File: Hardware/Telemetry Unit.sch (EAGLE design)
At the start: 51 parts, among them IC1 MEGA128-A, IC2 FT232RL, J2 503182-1852, J3 10118193-0001LF, Q1 10MHz, U1 MPL3115A2, U2 AP65111A, U3 LSM6DS3

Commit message: Added fuse to usb
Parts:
- added F1: MF-MSMF050-2, MF-MSMF050-2:MF-MSMF050-2
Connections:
- new net N$22: F1.1, J3.VUSB
- net V_USB: now also F1.2; no longer J3.VUSB
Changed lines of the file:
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@@
 <?xml version="1.0" encoding="utf-8"?>
 <!DOCTYPE eagle SYSTEM "eagle.dtd">
-<eagle version="9.2.2">
+<eagle version="9.3.0">
 <drawing>
 <settings>
@@
 <part name="R15" library="resistor" library_urn="urn:adsk.eagle:library:348" deviceset="R-US_" device="R0603" package3d_urn="urn:adsk.eagle:package:23555/3" value="10k"/>
 <part name="R16" library="resistor" library_urn="urn:adsk.eagle:library:348" deviceset="R-US_" device="R0603" package3d_urn="urn:adsk.eagle:package:23555/3" value="10k"/>
+<part name="F1" library="MF-MSMF050-2" deviceset="MF-MSMF050-2" device=""/>
 </parts>
 <sheets>
@@
 <attribute name="VALUE" x="21.59" y="70.358" size="1.778" layer="96"/>
 </instance>
+<instance part="F1" gate="G$1" x="-55.88" y="50.8" smashed="yes">
+<attribute name="NAME" x="-59.69661875" y="52.19943125" size="1.781090625" layer="95"/>
+<attribute name="VALUE" x="-59.696859375" y="47.873740625" size="1.7812" layer="96"/>
+</instance>
 </instances>
 <busses>
@@
 </segment>
 </net>
-<net name="V_USB" class="0">
-<segment>
-<pinref part="J3" gate="G$1" pin="VUSB"/>
-<wire x1="-63.5" y1="50.8" x2="-50.8" y2="50.8" width="0.1524" layer="91"/>
-<label x="-53.34" y="50.8" size="1.778" layer="95" align="bottom-right"/>
-</segment>
-</net>
 <net name="N$11" class="0">
 <segment>
@@
 </segment>
 </net>
+<net name="N$22" class="0">
+<segment>
+<pinref part="J3" gate="G$1" pin="VUSB"/>
+<pinref part="F1" gate="G$1" pin="1"/>
+<wire x1="-63.5" y1="50.8" x2="-60.96" y2="50.8" width="0.1524" layer="91"/>
+</segment>
+</net>
+<net name="V_USB" class="0">
+<segment>
+<pinref part="F1" gate="G$1" pin="2"/>
+<wire x1="-50.8" y1="50.8" x2="-45.72" y2="50.8" width="0.1524" layer="91"/>
+<label x="-48.26" y="50.8" size="1.778" layer="95"/>
+</segment>
+</net>

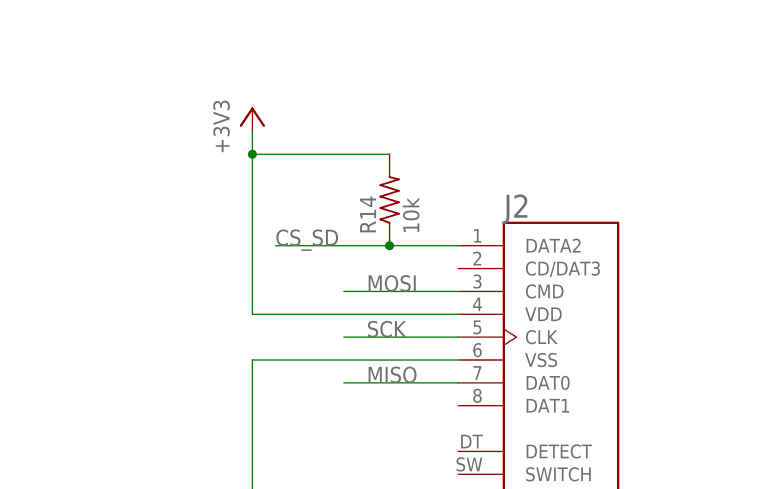
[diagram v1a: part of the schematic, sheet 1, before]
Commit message: Consolidated resistors and capacitors
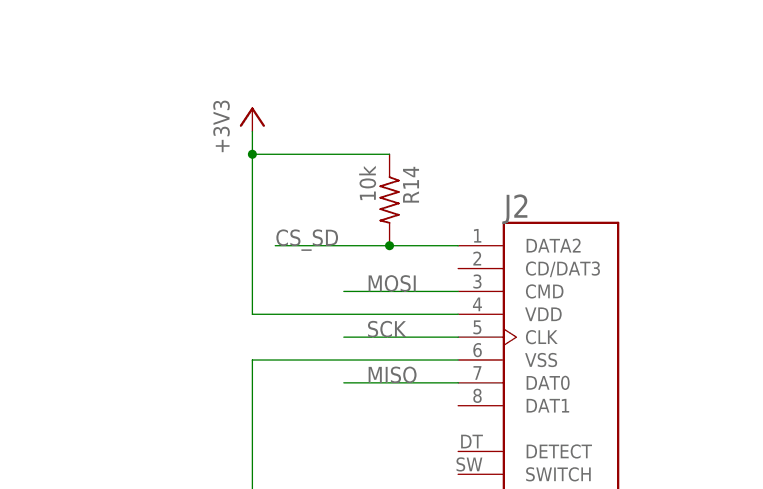
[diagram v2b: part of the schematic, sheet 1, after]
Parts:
- C14: value 100nF -> 100n; device rcl:C-EUC0603 -> resistor:C-USC0603
- R14: device rcl:R-US_R0603 -> resistor:R-US_R0603
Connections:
- net +3V3: now also R14.1; no longer R14.2
- net CS_SD: now also R14.2; no longer R14.1
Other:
- moved on the sheet: R14
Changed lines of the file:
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@@
 <part name="P+2" library="supply1" library_urn="urn:adsk.eagle:library:371" deviceset="+3V3" device=""/>
 <part name="GND17" library="supply1" library_urn="urn:adsk.eagle:library:371" deviceset="GND" device=""/>
-<part name="C14" library="rcl" library_urn="urn:adsk.eagle:library:334" deviceset="C-EU" device="C0603" package3d_urn="urn:adsk.eagle:package:23616/2" value="100nF"/>
 <part name="R12" library="rcl" library_urn="urn:adsk.eagle:library:334" deviceset="R-US_" device="R0603" package3d_urn="urn:adsk.eagle:package:23555/2" value="1k"/>
 <part name="R13" library="rcl" library_urn="urn:adsk.eagle:library:334" deviceset="R-US_" device="R0603" package3d_urn="urn:adsk.eagle:package:23555/2" value="1k"/>
@@
 <part name="P+3" library="supply1" library_urn="urn:adsk.eagle:library:371" deviceset="+3V3" device=""/>
 <part name="P+4" library="supply1" library_urn="urn:adsk.eagle:library:371" deviceset="+3V3" device=""/>
-<part name="R14" library="rcl" library_urn="urn:adsk.eagle:library:334" deviceset="R-US_" device="R0603" package3d_urn="urn:adsk.eagle:package:23555/2" value="10k"/>
 <part name="GND18" library="supply1" library_urn="urn:adsk.eagle:library:371" deviceset="GND" device=""/>
 <part name="JP1" library="pinhead" library_urn="urn:adsk.eagle:library:325" deviceset="PINHD-2X3" device="" package3d_urn="urn:adsk.eagle:package:22462/2"/>
@@
 <part name="R16" library="resistor" library_urn="urn:adsk.eagle:library:348" deviceset="R-US_" device="R0603" package3d_urn="urn:adsk.eagle:package:23555/3" value="10k"/>
 <part name="F1" library="MF-MSMF050-2" deviceset="MF-MSMF050-2" device=""/>
+<part name="R14" library="resistor" library_urn="urn:adsk.eagle:library:348" deviceset="R-US_" device="R0603" package3d_urn="urn:adsk.eagle:package:23555/3" value="10k"/>
+<part name="C14" library="resistor" library_urn="urn:adsk.eagle:library:348" deviceset="C-US" device="C0603" package3d_urn="urn:adsk.eagle:package:23616/2" value="100n"/>
 </parts>
 <sheets>
@@
 <attribute name="VALUE" x="127" y="68.58" size="1.778" layer="96"/>
 </instance>
-<instance part="R14" gate="G$1" x="144.78" y="116.84" smashed="yes" rot="R90">
-<attribute name="NAME" x="143.2814" y="113.03" size="1.778" layer="95" rot="R90"/>
-<attribute name="VALUE" x="148.082" y="113.03" size="1.778" layer="96" rot="R90"/>
+<instance part="R14" gate="G$1" x="144.78" y="116.84" smashed="yes" rot="R270">
+<attribute name="NAME" x="146.2786" y="120.65" size="1.778" layer="95" rot="R270"/>
+<attribute name="VALUE" x="141.478" y="120.65" size="1.778" layer="96" rot="R270"/>
 </instance>
 </instances>
@@
 <pinref part="+3V9" gate="G$1" pin="+3V3"/>
 <wire x1="129.54" y1="104.14" x2="129.54" y2="121.92" width="0.1524" layer="91"/>
-<pinref part="R14" gate="G$1" pin="2"/>
 <wire x1="129.54" y1="121.92" x2="129.54" y2="124.46" width="0.1524" layer="91"/>
 <wire x1="144.78" y1="121.92" x2="129.54" y2="121.92" width="0.1524" layer="91"/>
 <junction x="129.54" y="121.92"/>
+<pinref part="R14" gate="G$1" pin="1"/>
 </segment>
 </net>
@@
 </segment>
 <segment>
-<pinref part="R14" gate="G$1" pin="1"/>
 <pinref part="J2" gate="G$1" pin="DATA2"/>
-<wire x1="144.78" y1="111.76" x2="152.4" y2="111.76" width="0.1524" layer="91"/>
+<wire x1="152.4" y1="111.76" x2="144.78" y2="111.76" width="0.1524" layer="91"/>
+<label x="132.08" y="111.76" size="1.778" layer="95"/>
+<pinref part="R14" gate="G$1" pin="2"/>
 <wire x1="144.78" y1="111.76" x2="132.08" y2="111.76" width="0.1524" layer="91"/>
 <junction x="144.78" y="111.76"/>
-<label x="132.08" y="111.76" size="1.778" layer="95"/>
 </segment>
 </net>
@@
 <attribute name="VALUE" x="-33.02" y="22.86" size="1.778" layer="96"/>
 </instance>
-<instance part="C14" gate="G$1" x="25.4" y="66.04" smashed="yes" rot="R90">
-<attribute name="NAME" x="23.876" y="65.659" size="1.778" layer="95" rot="R180"/>
-<attribute name="VALUE" x="26.416" y="63.119" size="1.778" layer="96" rot="R180"/>
-</instance>
 <instance part="R12" gate="G$1" x="20.32" y="43.18" smashed="yes" rot="R90">
 <attribute name="NAME" x="18.8214" y="39.37" size="1.778" layer="95" rot="R90"/>
@@
 <attribute name="NAME" x="-59.69661875" y="52.19943125" size="1.781090625" layer="95"/>
 <attribute name="VALUE" x="-59.696859375" y="47.873740625" size="1.7812" layer="96"/>
+</instance>
+<instance part="C14" gate="G$1" x="25.4" y="66.04" smashed="yes" rot="R90">
+<attribute name="NAME" x="24.765" y="67.056" size="1.778" layer="95" rot="R90"/>
+<attribute name="VALUE" x="29.591" y="67.056" size="1.778" layer="96" rot="R90"/>
 </instance>
 </instances>
@@
 <net name="N$16" class="0">
 <segment>
-<pinref part="C14" gate="G$1" pin="1"/>
 <pinref part="IC2" gate="1" pin="!DTR"/>
 <wire x1="22.86" y1="66.04" x2="5.08" y2="66.04" width="0.1524" layer="91"/>
+<pinref part="C14" gate="G$1" pin="1"/>
 </segment>
 </net>
@@
 <net name="RST2" class="0">
 <segment>
-<pinref part="C14" gate="G$1" pin="2"/>
 <wire x1="30.48" y1="66.04" x2="35.56" y2="66.04" width="0.1524" layer="91"/>
 <label x="33.02" y="66.04" size="1.778" layer="95"/>
-</segment>
-<segment>
+<pinref part="C14" gate="G$1" pin="2"/>
+</segment>
+<segment>

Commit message: Most minor updates and some rerouting
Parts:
- R11, R2: value 470 -> 1k
- R16: value 10k -> 330
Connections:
- removed net N$21: IC2.RXD, R16.1
- removed net RST2: C14.2, JP1.5, R1.2, S1.1@B
- removed net RX0: IC1.(RXD/PDI)PE0, R15.2, XB1.DOUT
- removed net TX0: IC1.(TXD/PDO)PE1, R16.2, XB1.DIN/!CONFIG
- new net ALT_INT: IC1.(OC3B/INT4)PE4, U1.INT1
- new net PDI: JP1.4, R16.1
- new net RX0/PDI: IC1.(RXD/PDI)PE0, R15.2, R16.2, XB1.DOUT
- new net TX0/PDO: IC1.(TXD/PDO)PE1, IC2.RXD, JP1.1, XB1.DIN/!CONFIG
- net !RST: now also C14.2, JP1.5, R1.2
- net +3V3: no longer IC2.VCC
- net ACCEL_INT: now also IC1.(OC3C/INT5)PE5; no longer IC1.(OC3B/INT4)PE4
- net CS_SD: now also J2.CD/DAT3; no longer J2.DATA2
- net GND: now also U3.CS, U3.SCX, U3.SDO/SA0, U3.SDX; no longer IC2.!RESET, S1.0@B
- net MISO: no longer JP1.1
- net MOSI: no longer JP1.4
- net V_USB: now also IC2.VCC
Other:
- moved on the sheet: R16

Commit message: New diode, layer cleanup, update silk
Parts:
- D1: device diode:DIODE-DO214AC -> diode:DIODE-SOD123
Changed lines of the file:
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@@
 <part name="+3V7" library="supply1" library_urn="urn:adsk.eagle:library:371" deviceset="+3V3" device=""/>
 <part name="GND13" library="supply1" library_urn="urn:adsk.eagle:library:371" deviceset="GND" device=""/>
-<part name="D1" library="diode" library_urn="urn:adsk.eagle:library:210" deviceset="DIODE-" device="DO214AC" package3d_urn="urn:adsk.eagle:package:43417/2"/>
+<part name="D1" library="diode" library_urn="urn:adsk.eagle:library:210" deviceset="DIODE-" device="SOD123" package3d_urn="urn:adsk.eagle:package:43420/1"/>
 <part name="U1" library="TrackerPeripherals" deviceset="MPL3115A2" device=""/>
 <part name="J1" library="TrackerPeripherals" deviceset="ST_2X1" device=""/>

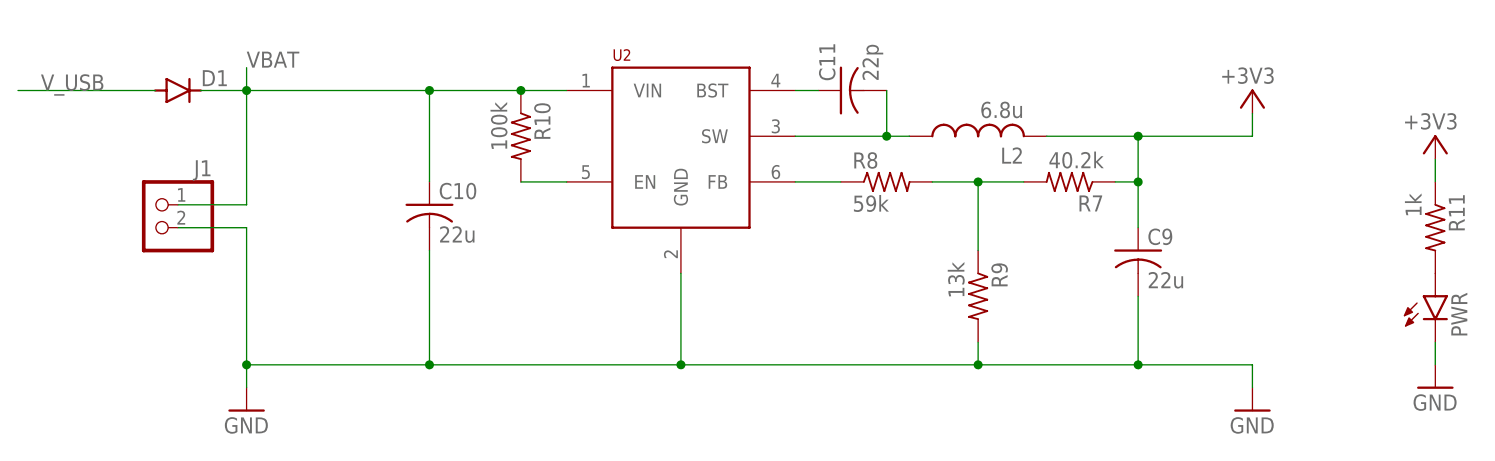
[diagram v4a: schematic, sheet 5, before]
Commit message: Replace voltage regulator, reroute all
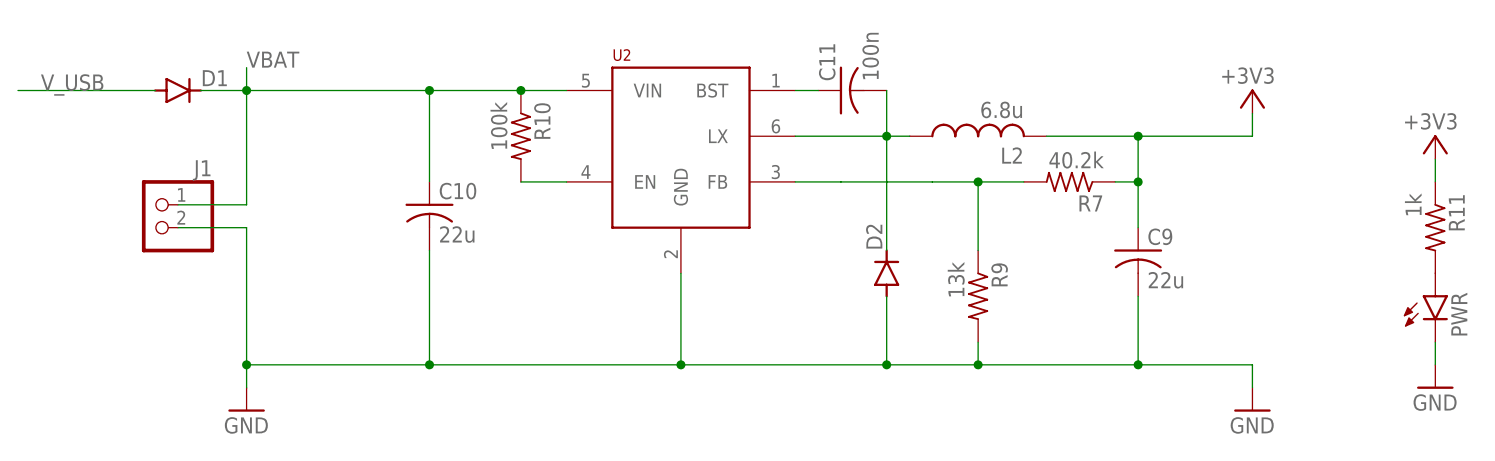
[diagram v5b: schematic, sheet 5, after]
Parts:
- removed R8: 59k, resistor:R-US_R0603
- added D2: (no value), diode:DIODE-SOD123
- C11: value 22p -> 100n
- U2: value AP65111A -> AOZ1280; device TrackerPeripherals:AP65111A -> TrackerPeripherals:AOZ1280
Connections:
- removed net N$8: R7.2, R8.2, R9.1
- net GND: now also D2.A
- net N$10: now also R7.2, R9.1; no longer R8.1
- net N$7: now also D2.C, U2.LX; no longer U2.SW
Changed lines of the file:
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@@
 <part name="R6" library="resistor" library_urn="urn:adsk.eagle:library:348" deviceset="R-US_" device="R0603" package3d_urn="urn:adsk.eagle:package:23555/3" value="10k"/>
 <part name="GND10" library="supply1" library_urn="urn:adsk.eagle:library:371" deviceset="GND" device=""/>
-<part name="U2" library="TrackerPeripherals" deviceset="AP65111A" device=""/>
 <part name="L2" library="TrackerPeripherals" deviceset="L_SMALL" device="L1210" value="6.8u"/>
 <part name="R7" library="resistor" library_urn="urn:adsk.eagle:library:348" deviceset="R-US_" device="R0603" package3d_urn="urn:adsk.eagle:package:23555/3" value="40.2k"/>
-<part name="R8" library="resistor" library_urn="urn:adsk.eagle:library:348" deviceset="R-US_" device="R0603" package3d_urn="urn:adsk.eagle:package:23555/3" value="59k"/>
 <part name="R9" library="resistor" library_urn="urn:adsk.eagle:library:348" deviceset="R-US_" device="R0603" package3d_urn="urn:adsk.eagle:package:23555/3" value="13k"/>
 <part name="+3V1" library="supply1" library_urn="urn:adsk.eagle:library:371" deviceset="+3V3" device=""/>
 <part name="R10" library="resistor" library_urn="urn:adsk.eagle:library:348" deviceset="R-US_" device="R0603" package3d_urn="urn:adsk.eagle:package:23555/3" value="100k"/>
-<part name="C11" library="resistor" library_urn="urn:adsk.eagle:library:348" deviceset="C-US" device="C0603" package3d_urn="urn:adsk.eagle:package:23616/2" value="22p"/>
+<part name="C11" library="resistor" library_urn="urn:adsk.eagle:library:348" deviceset="C-US" device="C0603" package3d_urn="urn:adsk.eagle:package:23616/2" value="100n"/>
 <part name="C9" library="resistor" library_urn="urn:adsk.eagle:library:348" deviceset="C-US" device="C0805" package3d_urn="urn:adsk.eagle:package:23617/2" value="22u"/>
 <part name="C10" library="resistor" library_urn="urn:adsk.eagle:library:348" deviceset="C-US" device="C0805" package3d_urn="urn:adsk.eagle:package:23617/2" value="22u"/>
@@
 <part name="GND20" library="supply1" library_urn="urn:adsk.eagle:library:371" deviceset="GND" device=""/>
 <part name="S1" library="TrackerPeripherals" deviceset="TACT_SW_4.5MM" device=""/>
+<part name="D2" library="diode" library_urn="urn:adsk.eagle:library:210" deviceset="DIODE-" device="SOD123" package3d_urn="urn:adsk.eagle:package:43420/1"/>
+<part name="U2" library="TrackerPeripherals" deviceset="AOZ1280" device=""/>
 </parts>
 <sheets>
@@
 </plain>
 <instances>
-<instance part="U2" gate="G$1" x="0" y="25.4" smashed="yes">
-<attribute name="NAME" x="-7.62" y="33.782" size="1.27" layer="94"/>
-</instance>
 <instance part="L2" gate="G$1" x="33.02" y="25.4" smashed="yes" rot="R90">
 <attribute name="NAME" x="38.1" y="24.13" size="1.778" layer="95" rot="R180"/>
@@
 <attribute name="VALUE" x="46.99" y="23.622" size="1.778" layer="96" rot="R180"/>
 </instance>
-<instance part="R8" gate="G$1" x="22.86" y="20.32" smashed="yes">
-<attribute name="NAME" x="19.05" y="21.8186" size="1.778" layer="95"/>
-<attribute name="VALUE" x="19.05" y="17.018" size="1.778" layer="96"/>
-</instance>
 <instance part="R9" gate="G$1" x="33.02" y="7.62" smashed="yes" rot="R270">
 <attribute name="NAME" x="34.5186" y="11.43" size="1.778" layer="95" rot="R270"/>
@@
 <attribute name="NAME" x="-52.07" y="20.955" size="1.778" layer="95" rot="MR0"/>
 <attribute name="VALUE" x="-52.07" y="10.16" size="1.778" layer="96" rot="MR0"/>
+</instance>
+<instance part="D2" gate="G$1" x="22.86" y="10.16" smashed="yes" rot="R90">
+<attribute name="NAME" x="22.3774" y="12.7" size="1.778" layer="95" rot="R90"/>
+<attribute name="VALUE" x="25.1714" y="12.7" size="1.778" layer="96" rot="R90"/>
+</instance>
+<instance part="U2" gate="G$1" x="0" y="25.4" smashed="yes">
+<attribute name="NAME" x="-7.62" y="33.782" size="1.27" layer="94"/>
 </instance>
 </instances>
@@
 <net name="GND" class="0">
 <segment>
-<pinref part="U2" gate="G$1" pin="GND"/>
 <wire x1="0" y1="10.16" x2="0" y2="0" width="0.1524" layer="91"/>
 <wire x1="0" y1="0" x2="-27.94" y2="0" width="0.1524" layer="91"/>
 <junction x="0" y="0"/>
-<wire x1="0" y1="0" x2="33.02" y2="0" width="0.1524" layer="91"/>
+<wire x1="0" y1="0" x2="22.86" y2="0" width="0.1524" layer="91"/>
+<wire x1="22.86" y1="0" x2="33.02" y2="0" width="0.1524" layer="91"/>
 <wire x1="33.02" y1="0" x2="33.02" y2="2.54" width="0.1524" layer="91"/>
 <pinref part="R9" gate="G$1" pin="2"/>
@@
 <wire x1="-55.88" y1="15.24" x2="-48.26" y2="15.24" width="0.1524" layer="91"/>
 <wire x1="-48.26" y1="15.24" x2="-48.26" y2="0" width="0.1524" layer="91"/>
+<pinref part="D2" gate="G$1" pin="A"/>
+<wire x1="22.86" y1="7.62" x2="22.86" y2="0" width="0.1524" layer="91"/>
+<junction x="22.86" y="0"/>
+<pinref part="U2" gate="G$1" pin="GND"/>
 </segment>
 <segment>
@@
 <net name="N$10" class="0">
 <segment>
-<pinref part="R8" gate="G$1" pin="1"/>
+<wire x1="17.78" y1="20.32" x2="12.7" y2="20.32" width="0.1524" layer="91"/>
+<pinref part="R7" gate="G$1" pin="2"/>
+<wire x1="27.94" y1="20.32" x2="33.02" y2="20.32" width="0.1524" layer="91"/>
+<pinref part="R9" gate="G$1" pin="1"/>
+<wire x1="33.02" y1="20.32" x2="38.1" y2="20.32" width="0.1524" layer="91"/>
+<wire x1="33.02" y1="12.7" x2="33.02" y2="20.32" width="0.1524" layer="91"/>
+<junction x="33.02" y="20.32"/>
+<wire x1="17.78" y1="20.32" x2="27.94" y2="20.32" width="0.1524" layer="91"/>
 <pinref part="U2" gate="G$1" pin="FB"/>
-<wire x1="17.78" y1="20.32" x2="12.7" y2="20.32" width="0.1524" layer="91"/>
 </segment>
 </net>
 <net name="N$9" class="0">
 <segment>
-<pinref part="U2" gate="G$1" pin="EN"/>
 <pinref part="R10" gate="G$1" pin="2"/>
 <wire x1="-12.7" y1="20.32" x2="-17.78" y2="20.32" width="0.1524" layer="91"/>
+<pinref part="U2" gate="G$1" pin="EN"/>
 </segment>
 </net>
 <net name="VBAT" class="0">
 <segment>
-<pinref part="U2" gate="G$1" pin="VIN"/>
 <pinref part="R10" gate="G$1" pin="1"/>
 <wire x1="-12.7" y1="30.48" x2="-17.78" y2="30.48" width="0.1524" layer="91"/>
@@
 <wire x1="-55.88" y1="17.78" x2="-48.26" y2="17.78" width="0.1524" layer="91"/>
 <wire x1="-48.26" y1="17.78" x2="-48.26" y2="30.48" width="0.1524" layer="91"/>
+<pinref part="U2" gate="G$1" pin="VIN"/>
 </segment>
 </net>
@@
 <segment>
 <pinref part="C11" gate="G$1" pin="1"/>
+<wire x1="15.24" y1="30.48" x2="12.7" y2="30.48" width="0.1524" layer="91"/>
 <pinref part="U2" gate="G$1" pin="BST"/>
-<wire x1="15.24" y1="30.48" x2="12.7" y2="30.48" width="0.1524" layer="91"/>
 </segment>
 </net>
 <net name="N$7" class="0">
 <segment>
-<pinref part="U2" gate="G$1" pin="SW"/>
 <pinref part="L2" gate="G$1" pin="1"/>
 <wire x1="12.7" y1="25.4" x2="22.86" y2="25.4" width="0.1524" layer="91"/>
@@
 <wire x1="22.86" y1="30.48" x2="22.86" y2="25.4" width="0.1524" layer="91"/>
 <junction x="22.86" y="25.4"/>
+<pinref part="D2" gate="G$1" pin="C"/>
+<wire x1="22.86" y1="12.7" x2="22.86" y2="25.4" width="0.1524" layer="91"/>
+<pinref part="U2" gate="G$1" pin="LX"/>
 </segment>
 </net>
@@
 </segment>
 </net>
-<net name="N$8" class="0">
-<segment>
-<pinref part="R8" gate="G$1" pin="2"/>
-<pinref part="R7" gate="G$1" pin="2"/>
-<wire x1="27.94" y1="20.32" x2="33.02" y2="20.32" width="0.1524" layer="91"/>
-<pinref part="R9" gate="G$1" pin="1"/>
-<wire x1="33.02" y1="20.32" x2="38.1" y2="20.32" width="0.1524" layer="91"/>
-<wire x1="33.02" y1="12.7" x2="33.02" y2="20.32" width="0.1524" layer="91"/>
-<junction x="33.02" y="20.32"/>
-</segment>
-</net>
